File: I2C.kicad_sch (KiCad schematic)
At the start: 15 parts, among them J702 Conn_01x04

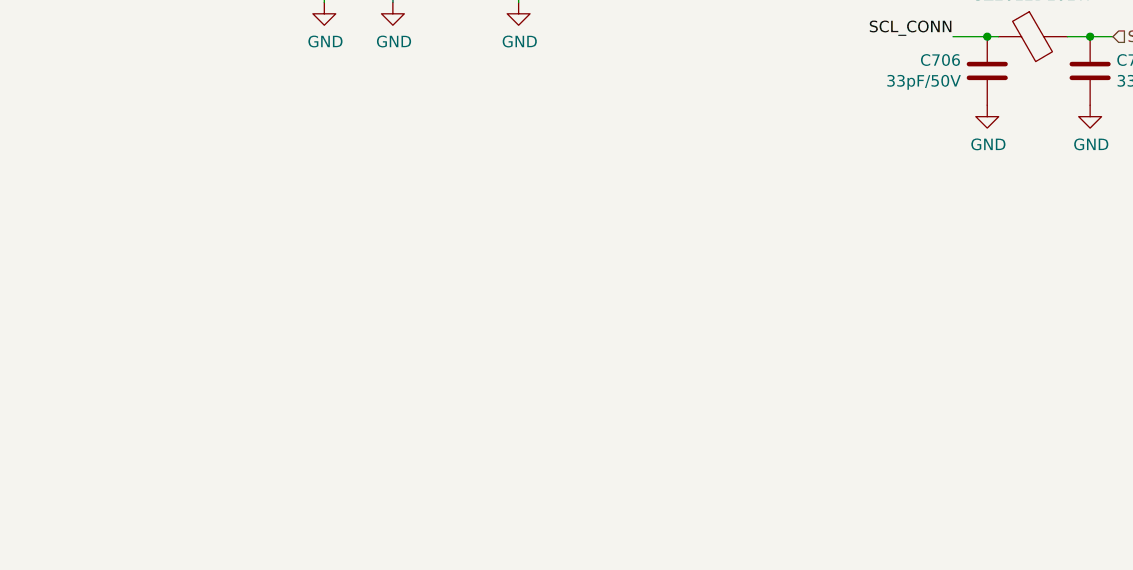
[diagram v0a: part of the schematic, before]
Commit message: Initial V1.0.0 Bluefin forked
Added ICM-42688-P 6-axis IMU
Added LM317 LDO for 6.4v or 5v MHU supply (selectable via jumper)
Added External LED's for IO2 (Pin 24) and 3.3v
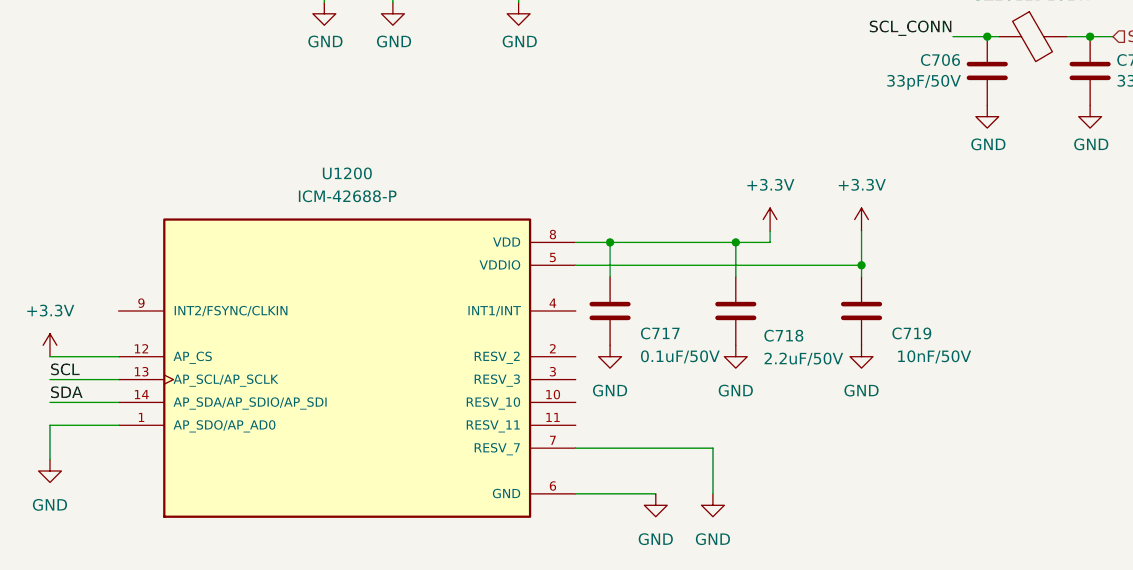
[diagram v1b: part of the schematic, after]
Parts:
- added C717: 0.1uF/50V, Capacitor_SMD:C_1206_3216Metric, symbol Device:C
- added C718: 2.2uF/50V, Capacitor_SMD:C_1206_3216Metric, symbol Device:C
- added C719: 10nF/50V, Capacitor_SMD:C_1206_3216Metric, symbol Device:C
- added U1200: ICM-42688-P, BLUEFIN:PQFN50P300X250X97-14N, symbol ICM-42688-P:ICM-42688-P
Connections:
- net +3.3V: now also C717.1, C718.1, C719.1, U1200.12 (AP_CS), U1200.5 (VDDIO), U1200.8 (VDD)
- net GND: now also C717.2, C718.2, C719.2, U1200.1 (AP_SDO/AP_AD0), U1200.6 (GND), U1200.7 (RESV_7)
- net SCL: now also U1200.13 (AP_SCL/AP_SCLK)
- net SDA: now also U1200.14 (AP_SDA/AP_SDIO/AP_SDI)

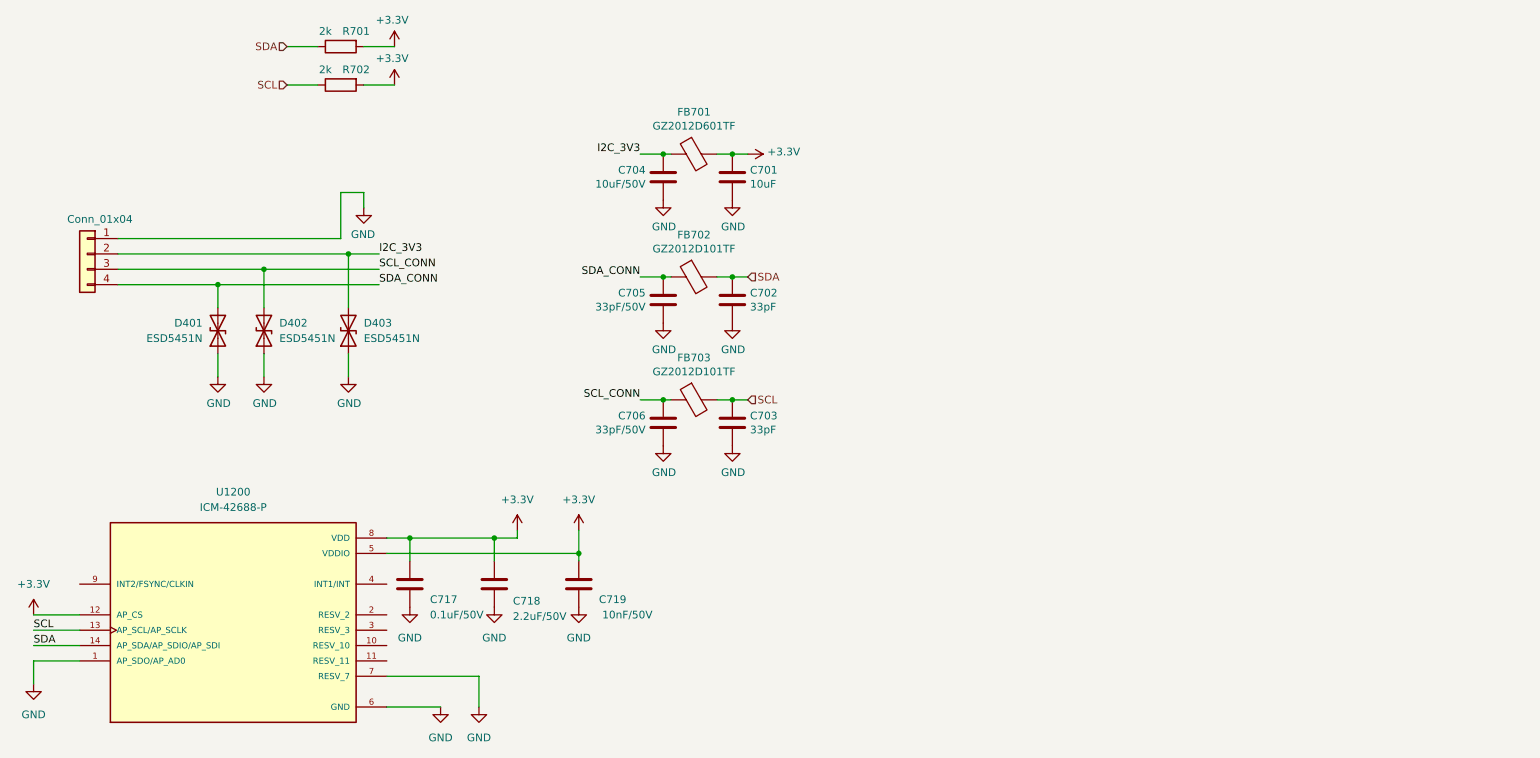
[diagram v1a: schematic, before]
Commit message: Updated LCSC part numbers
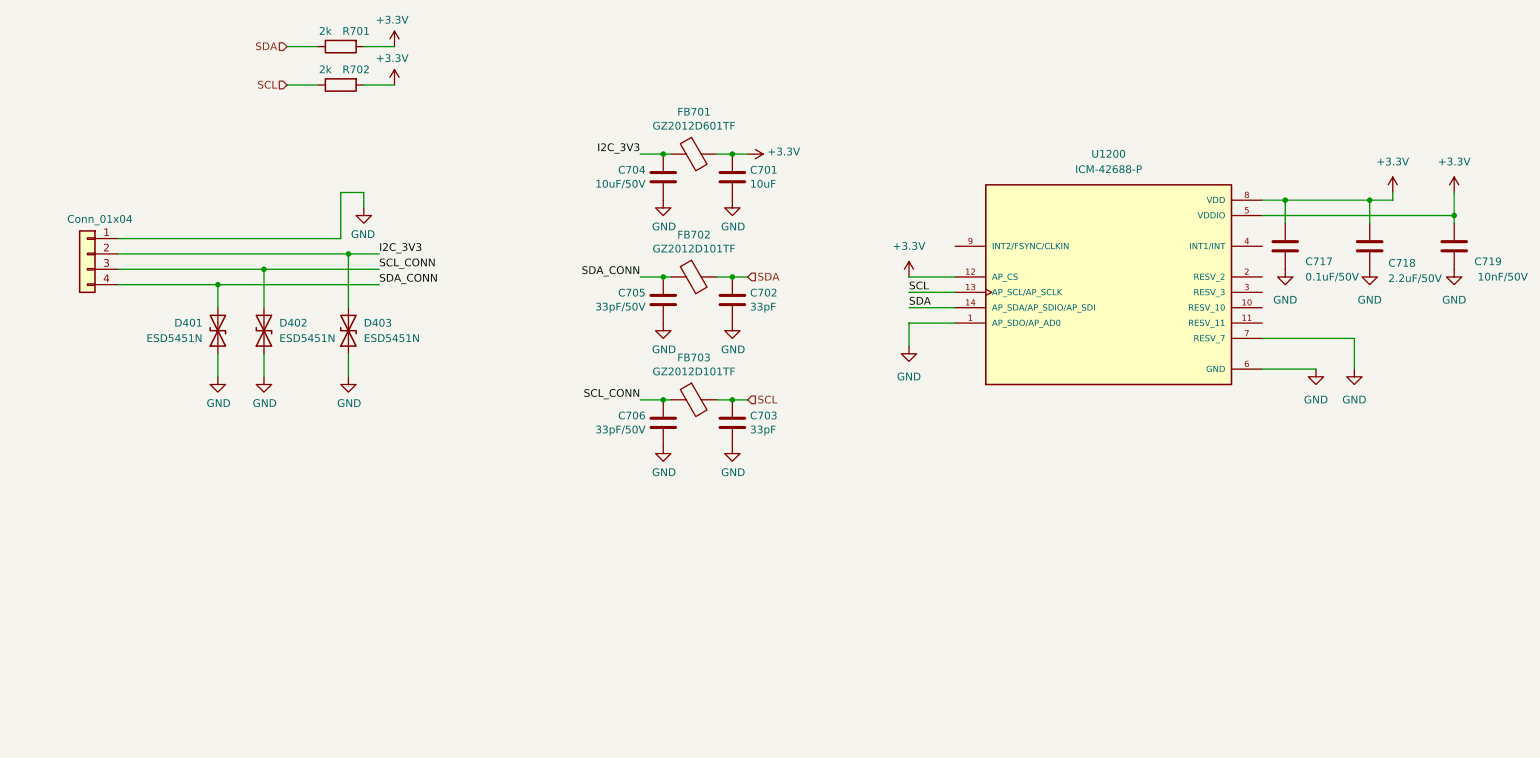
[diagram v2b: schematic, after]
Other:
- moved on the sheet: C717, C718, C719, U1200

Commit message: Moved ESP32-S3 + larger pin headers
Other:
- company: Hat Labs Ltd -> Fifty One North Limited
- title: Hat Labs Marine Engine & Tank interface (HALMET) -> Bluefin Marine Processor
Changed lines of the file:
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@@
 	(paper "A4")
 	(title_block
-		(title "Hat Labs Marine Engine & Tank interface (HALMET)")
-		(date "2024-01-18")
-		(rev "1.0.1")
-		(company "Hat Labs Ltd")
-		(comment 1 "https://creativecommons.org/licenses/by-sa/4.0")
-		(comment 2 "To view a copy of this license, visit ")
-		(comment 3 "HALMET is licensed under CC BY-SA 4.0.")
+		(title "Bluefin Marine Processor")
+		(date "2026-01-08")
+		(rev "1.0.0")
+		(company "Fifty One North Limited")
+		(comment 1 "https://creativecommons.org/licenses/by-sa/4.0/")
+		(comment 2 "Bluefin is licensed under CC BY-SA 4.0")
+		(comment 3 "Modifications © 2026 Fiftyone North Ltd.")
+		(comment 4 "Based on an original design by Hat Labs Ltd.")
 	)
 	(junction
